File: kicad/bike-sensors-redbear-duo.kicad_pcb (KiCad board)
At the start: 2 copper layers, 10 parts

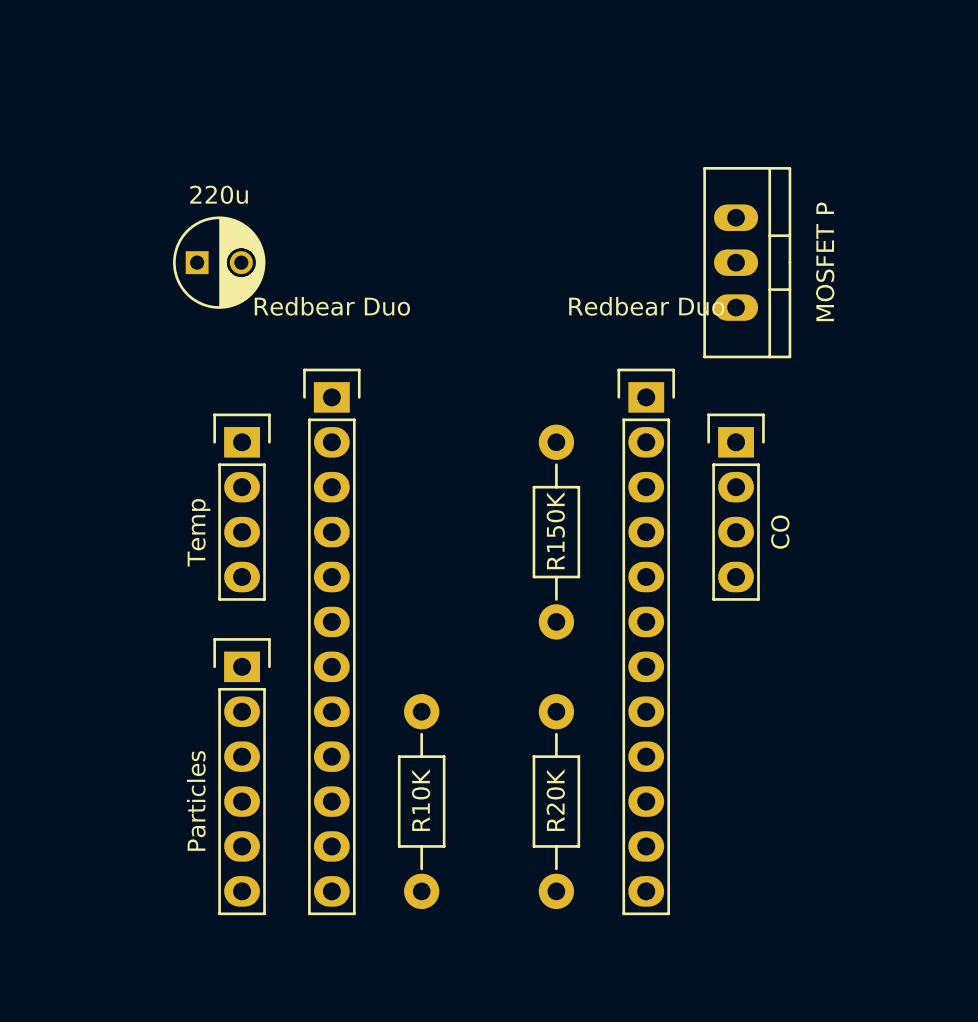
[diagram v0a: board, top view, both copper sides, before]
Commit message: Fixed the footprint. The magic was to append my custom RedbearDuo library to the Footprint Libraries Manager.
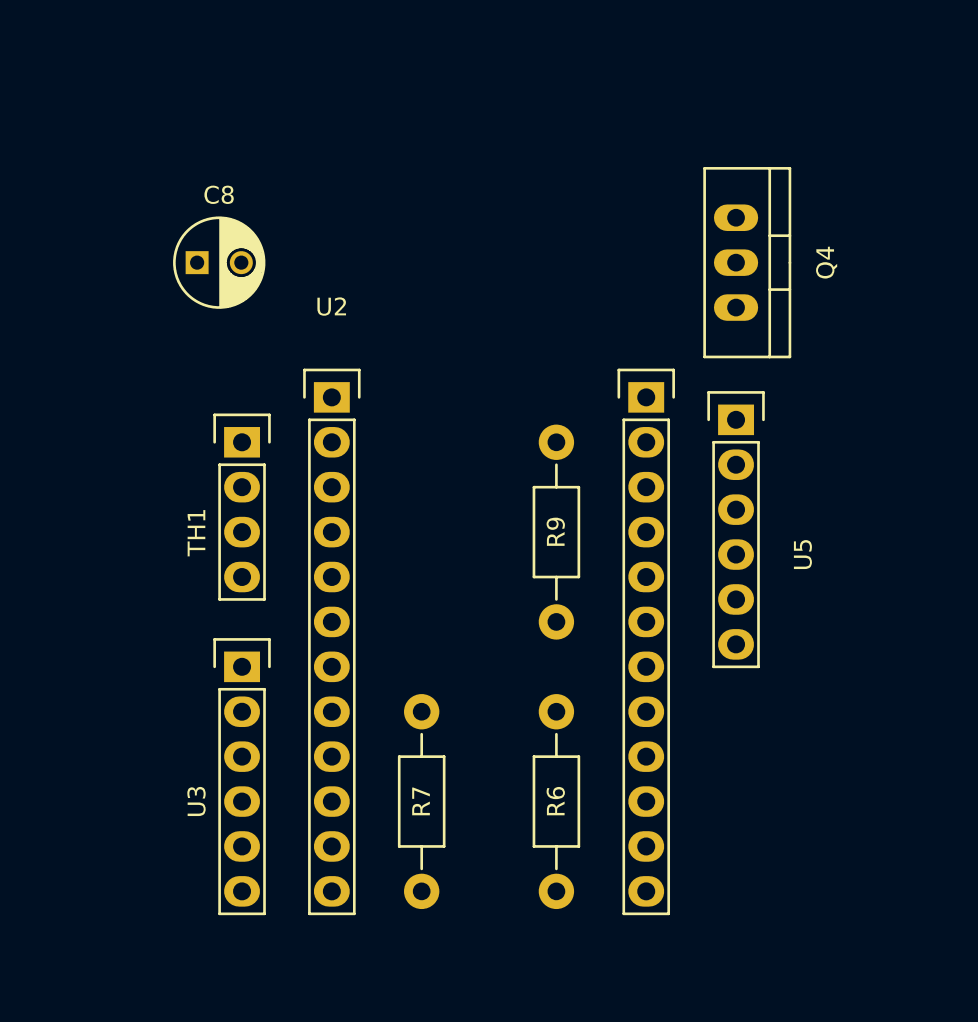
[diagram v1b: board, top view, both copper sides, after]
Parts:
- removed CO: Pin_Header_Straight_1x04, Pin_Headers:Pin_Header_Straight_1x04
- removed Redbear Duo: Pin_Header_Straight_1x12, Pin_Headers:Pin_Header_Straight_1x12 (x2)
- added U2: Redbear_Duo, RedbearDuo:RedbearDuo, F.Cu at (162.6, 78.7)
- added U5: MQ-7_Carbon_Monoxide, Pin_Headers:Pin_Header_Straight_1x06, F.Cu at (185.4, 80.0)
- C8: renamed from 220u; value C_Radial_D5_L6_P2.5 -> 220u
- Q4: renamed from MOSFET P; value TO-220_Neutral123_Vertical -> P_Channel_MOSFET
- R6: renamed from R20K; value Resistor_Horizontal_RM10mm -> R20K
- R7: renamed from R10K; value Resistor_Horizontal_RM10mm -> R10K
- R9: renamed from R150K; value Resistor_Horizontal_RM10mm -> R150
- TH1: renamed from Temp; value Pin_Header_Straight_1x04 -> DHT22_Temperature_Humidity
- U3: renamed from Particles; value Pin_Header_Straight_1x06 -> GP2Y10_Dust_Particulate
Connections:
- C8 pad 1: (no net) -> Net-(C8-Pad1)
- C8 pad 2: (no net) -> GND
- Q4 pad 1: (no net) -> Net-(Q4-Pad1)
- Q4 pad 2: (no net) -> Net-(Q4-Pad2)
- Q4 pad 3: (no net) -> Net-(Q4-Pad3)
- R6 pad 1: (no net) -> Net-(R6-Pad1)
- R6 pad 2: (no net) -> GND
- R7 pad 1: (no net) -> Net-(R7-Pad1)
- R7 pad 2: (no net) -> Net-(R7-Pad2)
- R9 pad 1: (no net) -> Net-(C8-Pad1)
- R9 pad 2: (no net) -> Net-(R9-Pad2)
- TH1 pad 1: (no net) -> Net-(R9-Pad2)
- TH1 pad 2: (no net) -> Net-(R7-Pad2)
- TH1 pad 3: (no net) -> Net-(TH1-Pad3)
- TH1 pad 4: (no net) -> GND
- U3 pad 1: (no net) -> Net-(C8-Pad1)
- U3 pad 2: (no net) -> GND
- U3 pad 3: (no net) -> Net-(U2-Pad24)
- U3 pad 4: (no net) -> GND
- U3 pad 5: (no net) -> Net-(U2-Pad22)
- U3 pad 6: (no net) -> Net-(R9-Pad2)

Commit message: Fixed the resistor junctions.
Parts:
- added HOLE1: MountingHole_3.2mm_M3, Mounting_Holes:MountingHole_3.2mm_M3, F.Cu at (152.4, 63.5)
- added HOLE2: MountingHole_3.2mm_M3, Mounting_Holes:MountingHole_3.2mm_M3, F.Cu at (190.5, 63.5)
- added HOLE3: MountingHole_3.2mm_M3, Mounting_Holes:MountingHole_3.2mm_M3, F.Cu at (152.4, 109.2)
- added HOLE4: MountingHole_3.2mm_M3, Mounting_Holes:MountingHole_3.2mm_M3, F.Cu at (190.5, 109.2)
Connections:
- R9 pad 2: Net-(R9-Pad2) -> Net-(R7-Pad1)
- TH1 pad 1: Net-(R9-Pad2) -> Net-(R7-Pad1)
- U2 pad 12: Net-(R9-Pad2) -> Net-(R7-Pad1)
- U2 pad 20: Net-(U2-Pad20) -> Net-(R6-Pad1)
- U3 pad 6: Net-(R9-Pad2) -> Net-(R7-Pad1)
- U5 pad 1: Net-(U2-Pad20) -> Net-(R6-Pad1)
- U5 pad 3: Net-(U2-Pad20) -> Net-(R6-Pad1)
- U5 pad 4: Net-(R9-Pad2) -> Net-(R7-Pad1)
- U5 pad 6: Net-(R9-Pad2) -> Net-(R7-Pad1)
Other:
- board outline added: 38.1 x 45.7 mm

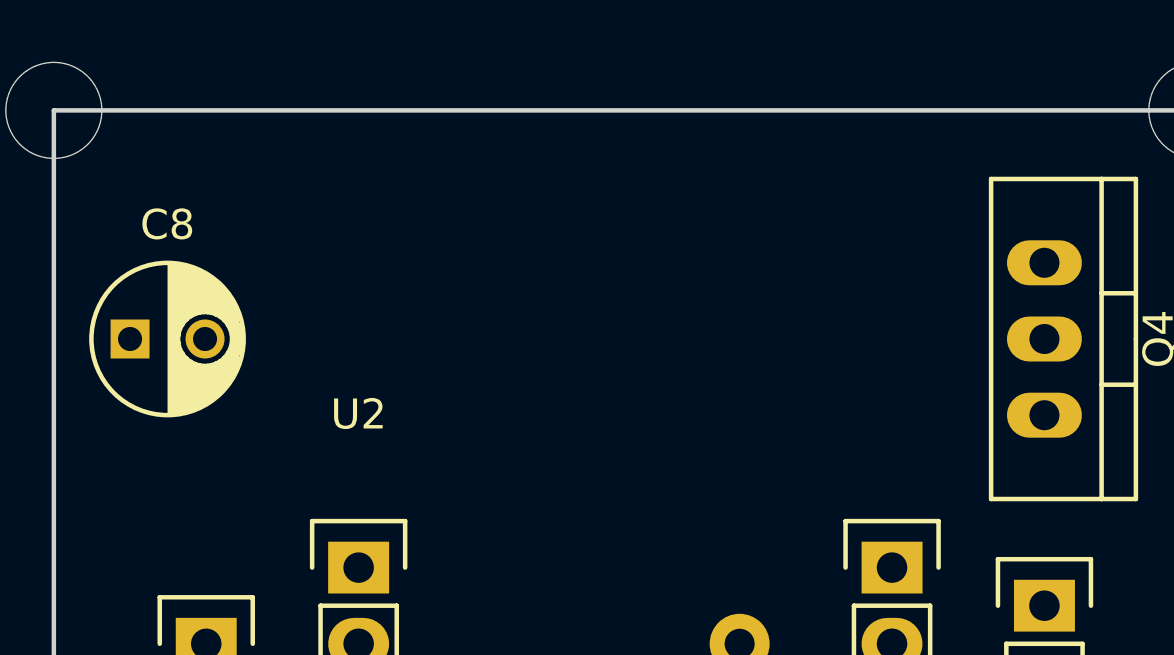
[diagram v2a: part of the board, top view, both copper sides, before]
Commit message: Added text to silk screen layer, and simple Hackerspace logo.
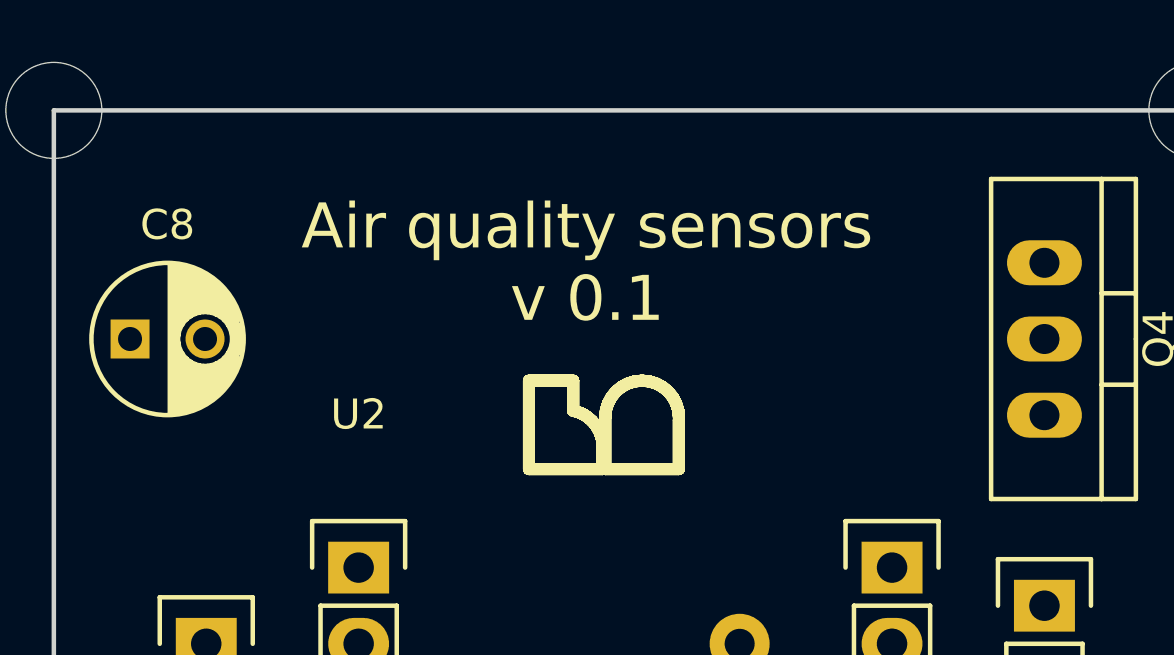
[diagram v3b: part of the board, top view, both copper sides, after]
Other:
- board text added: "Air quality sensors v 0.1"
- board text added: "Hackerspace Adelaide"
